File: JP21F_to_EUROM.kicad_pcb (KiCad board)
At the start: 2 copper layers, 58.4 x 24.8 mm, 2 parts, among them J1 SCART-F, J2 SCART-F

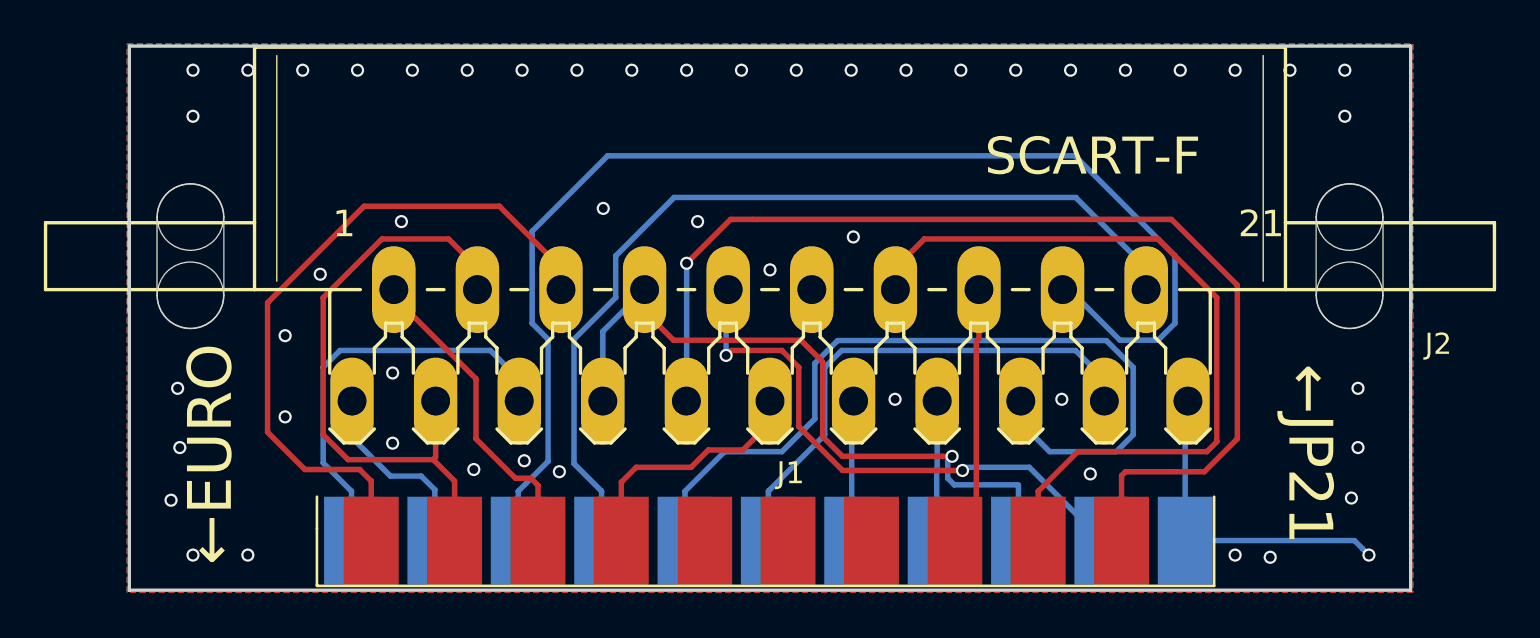
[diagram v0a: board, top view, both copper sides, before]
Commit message: fixed incorrect audio pins for JP21
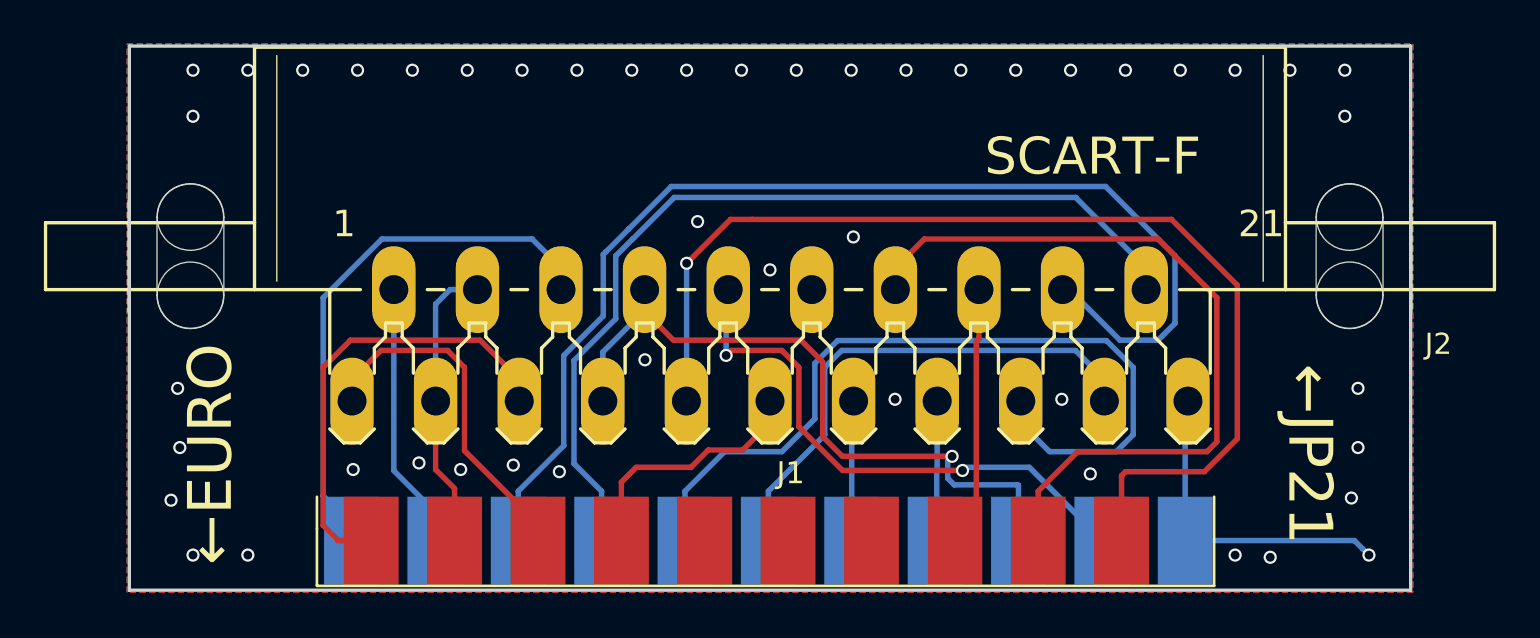
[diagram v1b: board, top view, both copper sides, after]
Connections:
- J2 pad 1: L_OUT -> L_IN
- J2 pad 2: L_IN -> L_OUT
- J2 pad 5: RT_OUT -> RT_IN
- J2 pad 6: RT_IN -> RT_OUT
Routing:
- net A_GND: track 29.2 -> 14.3 mm
- net RT_IN: track 31.6 -> 20.9 mm
- net RT_OUT: track 19.2 -> 25.1 mm
- net B_GND: track 57.8 -> 53.5 mm
- net L_OUT: track 8.74 -> 12.2 mm
- net L_IN: track 14.6 -> 16.3 mm
- net GND: vias 51 -> 47
